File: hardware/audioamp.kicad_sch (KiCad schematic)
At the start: 14 parts, among them J1 Conn_01x02_Pin, U8 PAM8302AAS

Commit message: Fixed some messed up labels (imports from EAGLE); cleaned up unused libs
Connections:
- net audio_out renamed pam8302_in
- net audio_sd renamed pam8302_sd
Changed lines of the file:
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@@
 		)
 	)
-	(hierarchical_label "audio_out"
+	(hierarchical_label "pam8302_in"
 		(shape input)
 		(at 121.92 60.96 180)
@@
 		)
 	)
-	(hierarchical_label "audio_sd"
+	(hierarchical_label "pam8302_sd"
 		(shape input)
 		(at 157.48 83.82 180)
@@
 			)
 		)
-		(property "Description" ""
+		(property "Description" "Power symbol creates a global label with name \"GND\" , ground"
 			(at 170.18 91.44 0)
 			(effects
@@
 			)
 		)
-		(property "Description" ""
+		(property "Description" "Unpolarized capacitor"
 			(at 128.27 73.66 0)
 			(effects
@@
 			)
 		)
-		(property "Description" ""
+		(property "Description" "Power symbol creates a global label with name \"+3.3VADC\""
 			(at 170.18 63.5 0)
 			(effects
@@
 			)
 		)
-		(property "Description" ""
+		(property "Description" "Unpolarized capacitor"
 			(at 217.17 72.39 0)
 			(effects
@@
 			)
 		)
-		(property "Description" ""
+		(property "Description" "Solder Jumper, 2-pole, closed/bridged"
 			(at 142.24 78.74 0)
 			(effects
@@
 			)
 		)
-		(property "Description" ""
+		(property "Description" "Power symbol creates a global label with name \"GND\" , ground"
 			(at 157.48 93.98 0)
 			(effects
@@
 			)
 		)
-		(property "Description" ""
+		(property "Description" "Power symbol creates a global label with name \"GND\" , ground"
 			(at 121.92 81.28 0)
 			(effects
@@
 			)
 		)
-		(property "Description" ""
+		(property "Description" "Solder Jumper, 2-pole, closed/bridged"
 			(at 142.24 73.66 0)
 			(effects
@@
 			)
 		)
-		(property "Description" ""
+		(property "Description" "Resistor"
 			(at 142.24 83.82 0)
 			(effects
@@
 			)
 		)
-		(property "Description" ""
+		(property "Description" "Resistor"
 			(at 142.24 68.58 0)
 			(effects
@@
 			)
 		)
-		(property "Description" ""
+		(property "Description" "Resistor"
 			(at 121.92 67.31 0)
 			(effects
@@
 			)
 		)
-		(property "Description" ""
+		(property "Description" "Resistor"
 			(at 121.92 74.93 0)
 			(effects
@@
 			)
 		)
-		(property "Description" ""
+		(property "Description" "Unpolarized capacitor"
 			(at 240.03 72.39 0)
 			(effects
@@
 			)
 		)
-		(property "Description" ""
+		(property "Description" "Unpolarized capacitor"
 			(at 228.6 72.39 0)
 			(effects
@@
 			)
 		)
-		(property "Description" ""
+		(property "Description" "Resistor"
 			(at 157.48 90.17 0)
 			(effects
@@
 			)
 		)
-		(property "Description" ""
+		(property "Description" "Power symbol creates a global label with name \"GND\" , ground"
 			(at 228.6 76.2 0)
 			(effects
@@
 			)
 		)
-		(property "Description" ""
+		(property "Description" "Power symbol creates a global label with name \"+3.3VADC\""
 			(at 228.6 68.58 0)
 			(effects
@@
 			)
 		)
-		(property "Description" ""
+		(property "Description" "Unpolarized capacitor"
 			(at 128.27 78.74 0)
 			(effects

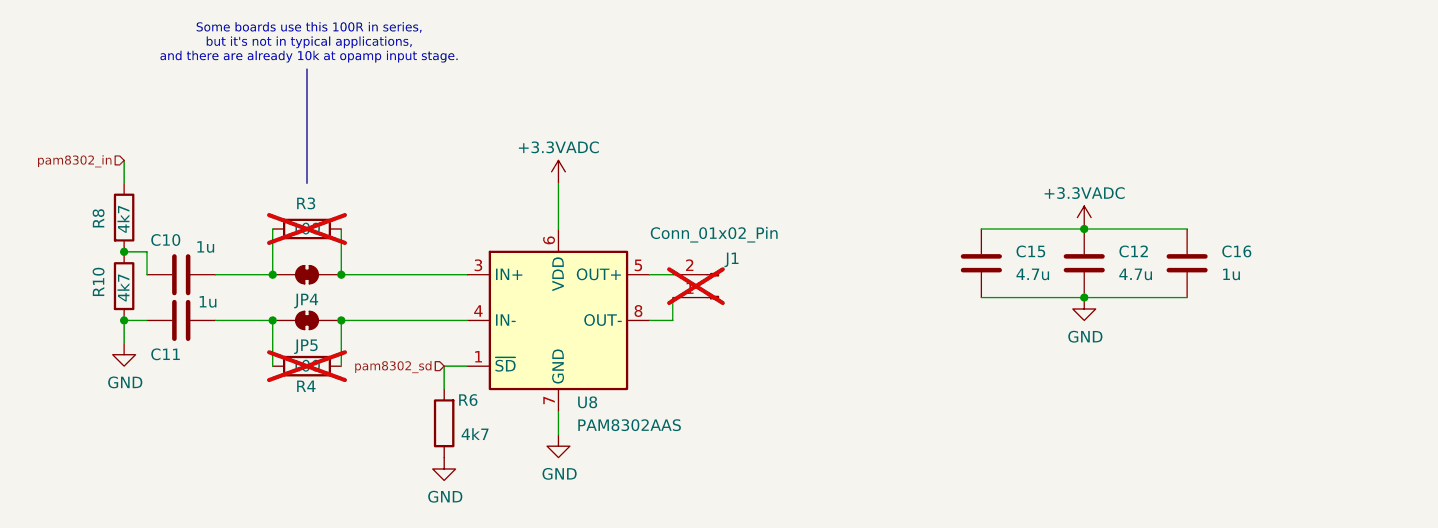
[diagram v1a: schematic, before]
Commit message: Replaced RJ12 connector value (not available anymore); cleanup of iBOM, removed unused old csv/ods BOM
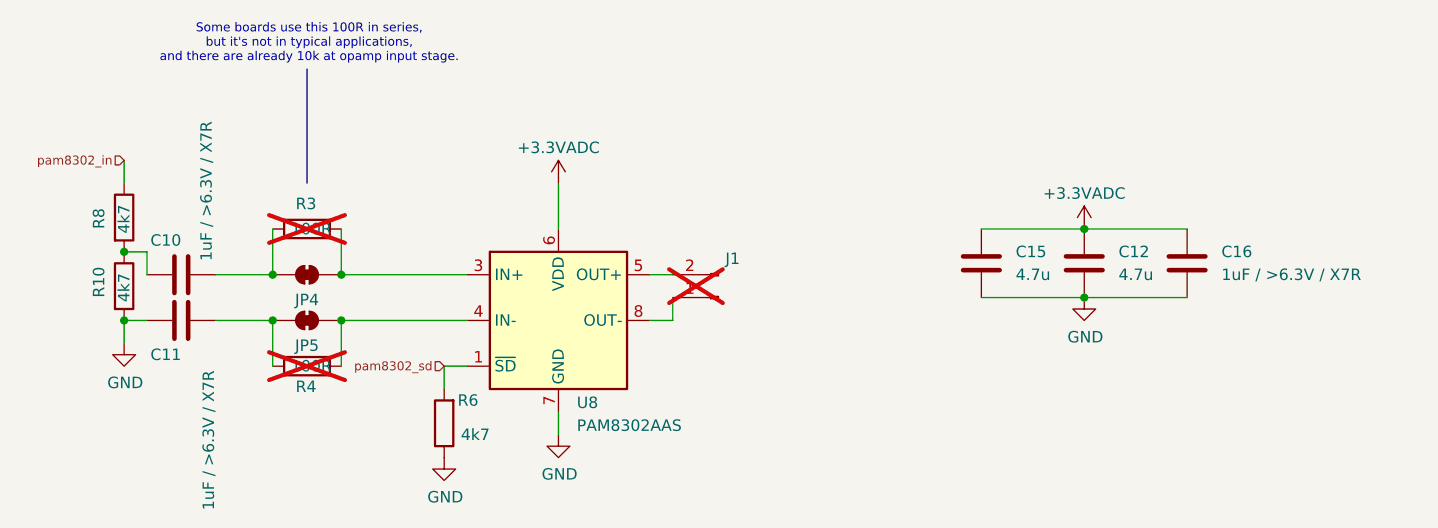
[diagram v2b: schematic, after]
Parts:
- C10, C11, C16: value 1u -> 1uF / >6.3V / X7R
- J1: value Conn_01x02_Pin -> ~
- R3, R4: value 100 -> 100R
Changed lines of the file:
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@@
 			)
 		)
-		(property "Value" "Conn_01x02_Pin"
+		(property "Value" "~"
 			(at 180.34 69.088 0)
 			(effects
@@
 			)
 		)
-		(property "Value" "1u"
-			(at 132.08 70.612 90)
+		(property "Value" "1uF / >6.3V / X7R"
+			(at 131.064 72.136 0)
 			(effects
 				(font
@@
 			)
 		)
-		(property "Value" "100"
+		(property "Value" "100R"
 			(at 140.462 83.82 90)
 			(effects
@@
 			)
 		)
-		(property "Value" "100"
+		(property "Value" "100R"
 			(at 140.462 68.58 90)
 			(effects
@@
 			)
 		)
-		(property "Value" "1u"
+		(property "Value" "1uF / >6.3V / X7R"
 			(at 243.84 73.6599 0)
 			(effects
@@
 			)
 		)
-		(property "Value" "1u"
-			(at 132.334 76.708 90)
-			(effects
-				(font
+		(property "Value" "1uF / >6.3V / X7R"
+			(at 131.318 99.822 0)
+			(effects
+				(font
